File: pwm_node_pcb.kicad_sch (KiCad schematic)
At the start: 36 parts, among them J1 External Power, J2 CAN1, U1 LD1117S33CTR, U2 TJA1051T/3, U3 AP63203WU, U4 TXB0104QPWRQ1, U5 STM32L432KCU

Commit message: Add re-layout WIP changes
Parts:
- removed C7: 22p, Capacitor_SMD:C_0603_1608Metric, symbol Device:C
- removed J2: CAN1, Connector_PinHeader_2.54mm:PinHeader_1x02_P2.54mm_Vertical, symbol Connector:Conn_01x02_Pin
- removed J3: ~, tag_connect:tag_connect_tc2030-idc-nl, symbol tag_connect:tag_connect_arm_swd_tc2030-nl
- removed L1: 10u, Inductor_SMD:L_0402_1005Metric, symbol Device:L
- removed U3: AP63203WU, Package_TO_SOT_SMD:TSOT-23-6, symbol Regulator_Switching:AP63203WU
- added J2: TC2050-IDC-NL, tag_connect:tag_connect_tc2050-idc-nl, symbol tag_connect:tag_connect_arm_swd_tc2050-nl
- added R4: 76k8, Resistor_SMD:R_0603_1608Metric, symbol Device:R
- added TP1: TestPoint, TestPoint:TestPoint_Pad_D1.5mm, symbol Connector:TestPoint
- added U3: TPSM82903, ti_buck:tpsm8290x, symbol ti_buck:tpsm82903
- C3: footprint Capacitor_SMD:C_0603_1608Metric -> Capacitor_SMD:C_0805_2012Metric
- C4: value 100n -> 22u; footprint Capacitor_SMD:C_0603_1608Metric -> Capacitor_SMD:C_0805_2012Metric
- C5: value 100p -> 16n
- C6: value 22p -> 4n7
- J1: value External Power -> CAN1
- R1: value 120R -> 60R
- R2: value 158k -> 60R
- R3: value 30k1 -> 76k8
- renumbered C11 to C10, C12 to C11, C8 to C7, C9 to C8, C10 to C9, J4 to J3, R4 to R5, U5 to U4, U4 to U5
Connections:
- net +3V3: now also J2.1 (VCC)
- net +5V: now also C4.1, J3.11, J3.2, J3.5, J3.8, U3.10 (VOUT), U3.9 (VOUT); no longer C5.1, C6.1, R2.1
- net CAN1+: now also J1.1 (Pin_1), R2.1; no longer R1.1
- net CAN1-: now also J1.2 (Pin_2), R1.1; no longer R1.2
- net GND: now also C4.2, C5.2, C6.2, J2.3 (GND), J2.5 (GND/VPROG), R4.2, U3.11 (GND); no longer J1.2 (Pin_2)
- net NRST: now also J2.10 (~{RESET})
- net SWCLK: now also J2.4 (SWCLK/TCK)
- net SWDIO: now also J2.2 (SWDIO/TMS)
- net SWO: now also J2.6 (SWO/TDO)
- removed net +V_{L}: C3.1, J1.1 (Pin_1), J3.11, J3.2, J3.5, J3.8
- new net: C6.1, R1.2, R2.2
- new net: TP1.1, U3.6 (PG)
- new net: C5.1, U3.5 (SS/TR)
- new net: R4.1, U3.4 (MODE/S-CONF)
- new net: R3.1, U3.7 (FB/VSET)
- new net +VSUPPLY: C3.1, U3.1 (VIN), U3.2 (VIN), U3.3 (EN)
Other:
- note added: "5V Buck Converter"
- note added: "MODE/S-CONFIG Resistor Setting: - FB/VSET-Pin: VSET mode - R_{MODE/S-CONF} = 76.8kΩ - F_{SW} = 1 MHz - Output discharge: Yes - Mode: Forced PWM - Dynamic mode change: Not active"
- note added: "Resistors: E96 Resistor Series, 1% Accuracy, Temperature Coefficient better or equal than ±200 ppm/°C C_{VIN} suggested: 0805 C_{VOUT} suggested: 0805"
- note added: "Soft start time C_{SS} = T_{SS} * I_{SS} / V_{REF} I_{SS} = 2.5uA V_{REF} = V_{FB}/0.75 V_{REF} = 0.6V / 0.75 = 0.8V For T_{SS} = 5ms: C_{SS} = 15.625nF"
- note added: "VSET Mode (5V) - R_{VSET} = 76.8kΩ"
- note removed: "Load Power Supply and to 5V"
- moved on the sheet: C10, C11, C7, C8, C9, JP1, JP2, R5, U4, U5

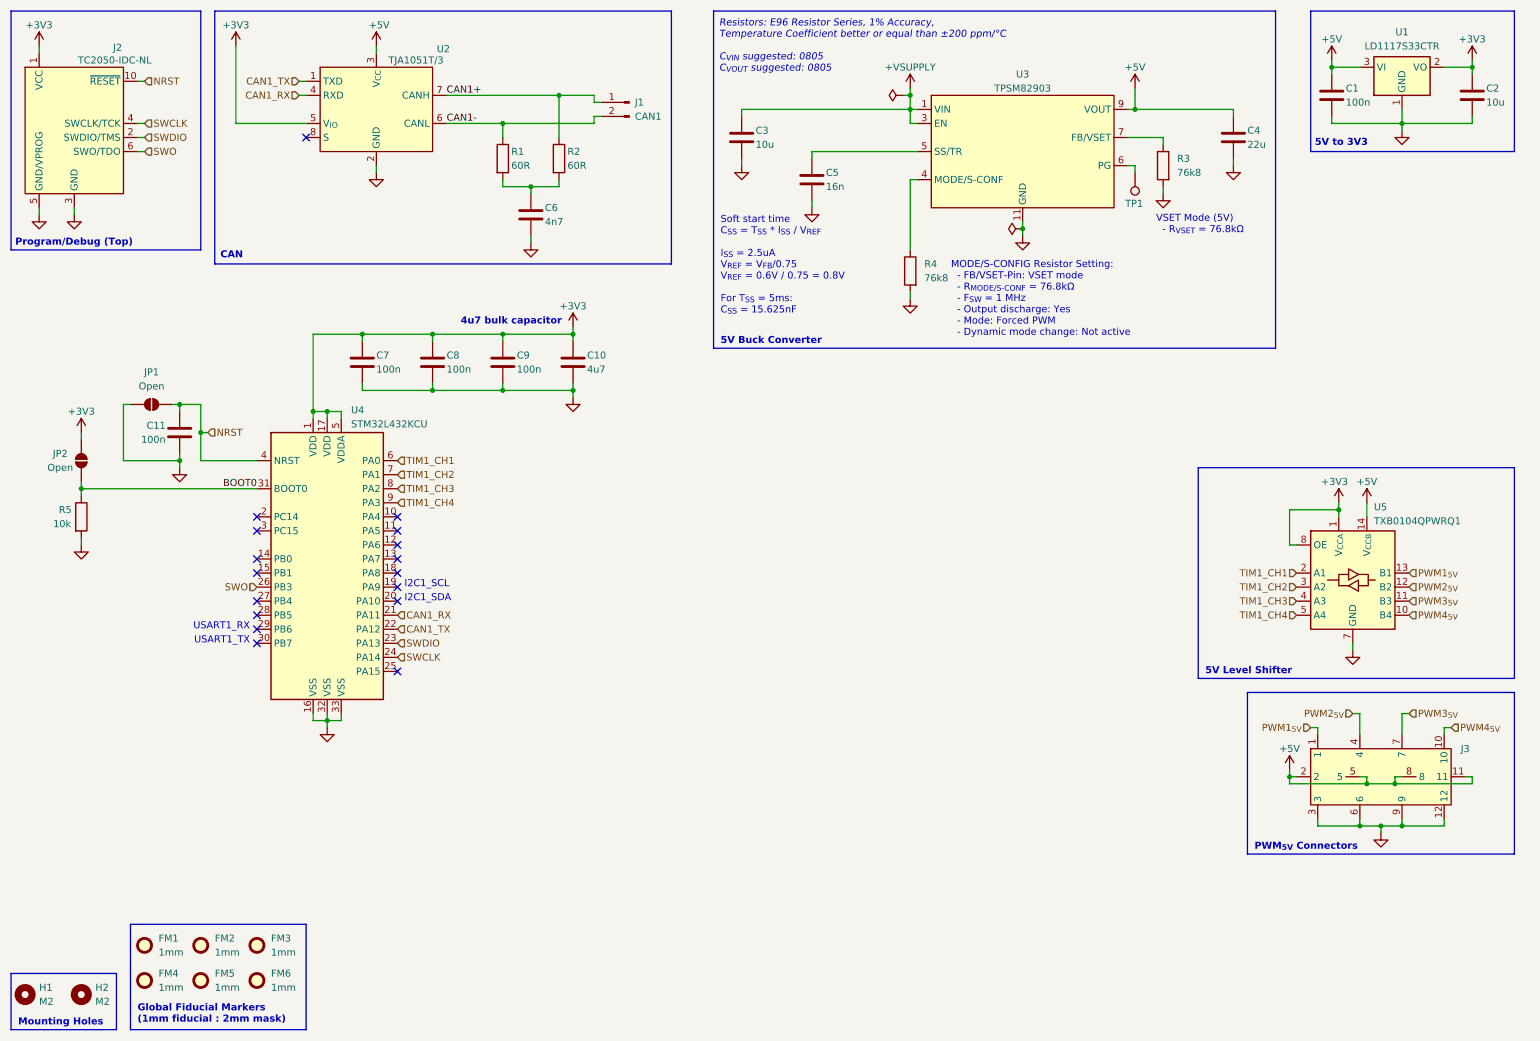
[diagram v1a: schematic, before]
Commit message: Revamp schematic and nuke PCB
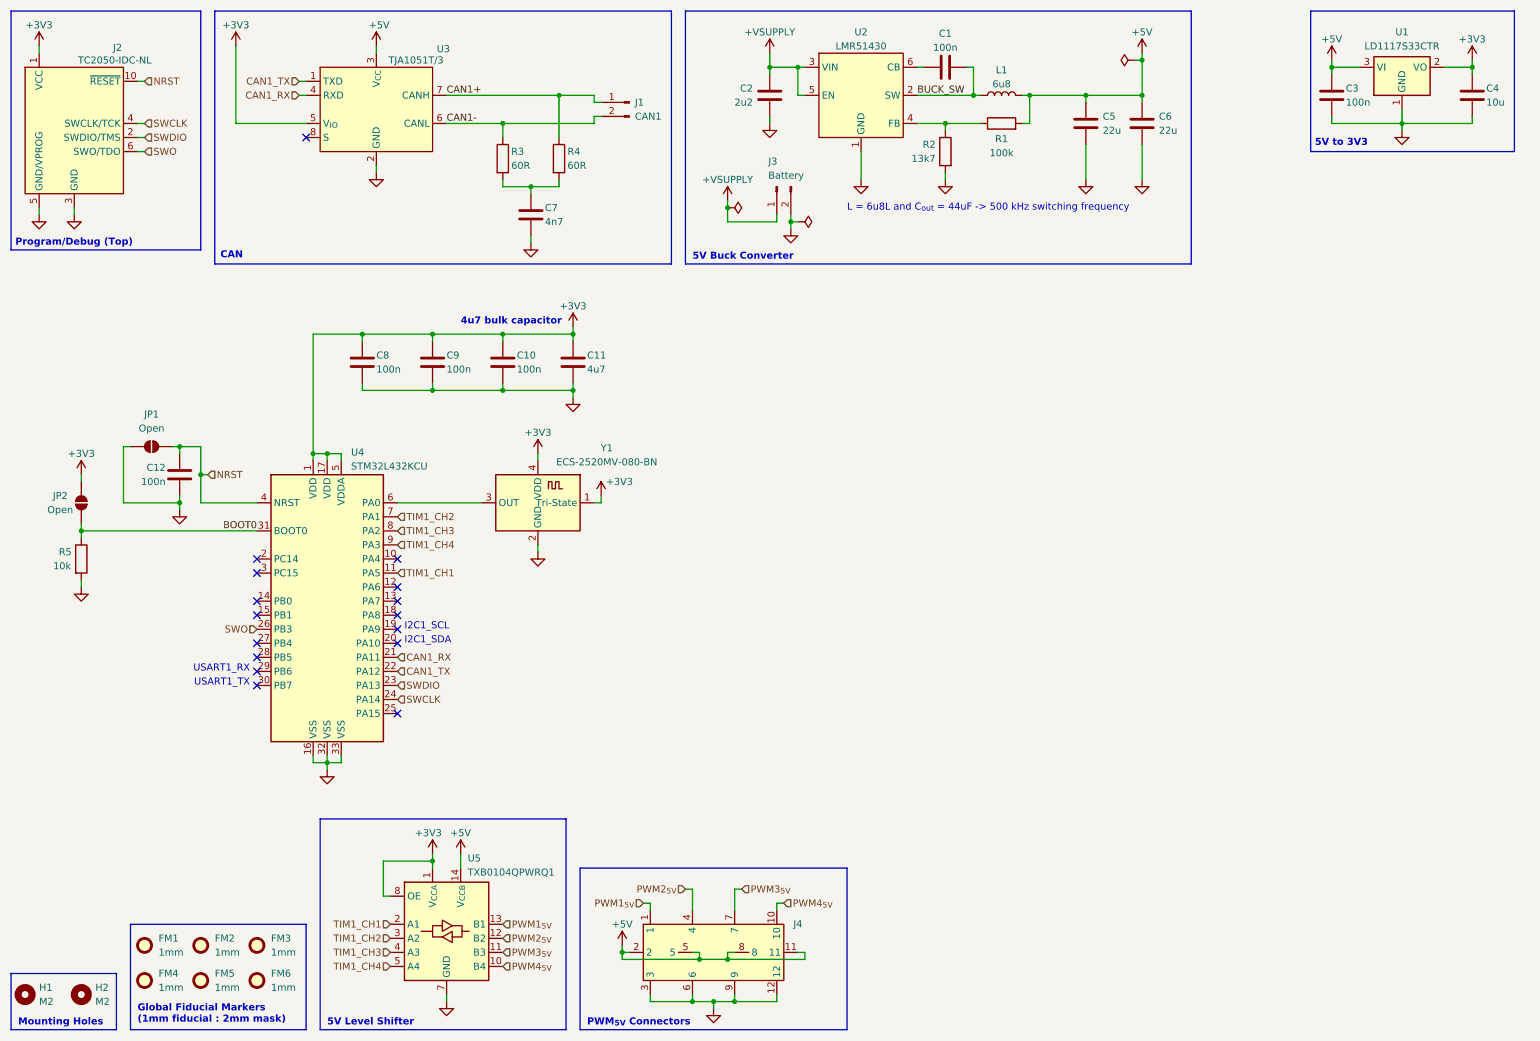
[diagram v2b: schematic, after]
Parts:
- removed C3: 10u, Capacitor_SMD:C_0805_2012Metric, symbol Device:C
- removed C4: 22u, Capacitor_SMD:C_0805_2012Metric, symbol Device:C
- removed J3: ~, pwm_node_connector:3x4_2-54mm_breakout, symbol pwm_node_connector:3x4_2-54mm_breakout
- removed R3, R4: 76k8, Resistor_SMD:R_0603_1608Metric, symbol Device:R
- removed TP1: TestPoint, TestPoint:TestPoint_Pad_D1.5mm, symbol Connector:TestPoint
- removed U3: TPSM82903, ti_buck:tpsm8290x, symbol ti_buck:tpsm82903
- added C1: 100n, Capacitor_SMD:C_0805_2012Metric, symbol Device:C
- added C2: 2u2, Capacitor_SMD:C_0805_2012Metric, symbol Device:C
- added C6: 22u, Capacitor_SMD:C_1210_3225Metric, symbol Device:C
- added J3: Battery, pwm_node_connectors:battery, symbol Connector:Conn_01x02_Pin
- added J4: ~, pwm_node_connectors:3x4_2-54mm_breakout, symbol pwm_connector_3x4_2-54mm_breakout:3x4_2-54mm_breakout
- added L1: 6u8, pwm_node_inductor:vishay_ihlp-2525cz, symbol Device:L
- added R1: 100k, Resistor_SMD:R_0603_1608Metric, symbol Device:R
- added R2: 13k7, Resistor_SMD:R_0603_1608Metric, symbol Device:R
- added U2: LMR51430, ti_buck:lmr51430, symbol ti_buck:lmr51430
- added Y1: ECS-2520MV-080-BN, Oscillator:Oscillator_SMD_ECS_2520MV-xxx-xx-4Pin_2.5x2.0mm, symbol Oscillator:ECS-2520MV-xxx-xx
- C5: value 16n -> 22u; footprint Capacitor_SMD:C_0603_1608Metric -> Capacitor_SMD:C_1210_3225Metric
- U4: Manufacturer Part Number STM32L432KC -> STM32L432KCU6
- renumbered C9 to C10, C10 to C11, C11 to C12, C1 to C3, C2 to C4, C6 to C7, C7 to C8, C8 to C9, R1 to R3, R2 to R4, U2 to U3
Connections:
- net +3V3: now also Y1.1 (Tri-State), Y1.4 (VDD)
- net +5V: now also C5.2, C6.2, J4.11, J4.2, J4.5, J4.8, L1.2, R1.2
- net +VSUPPLY: now also C2.1, J3.1 (Pin_1), U2.3 (VIN), U2.5 (EN)
- net GND: now also C5.1, C2.2, C6.1, J3.2 (Pin_2), J4.12, J4.3, J4.6, J4.9, R2.2, U2.1 (GND), Y1.2 (GND); no longer C5.2
- net PWM1_{5V}: now also J4.1
- net PWM2_{5V}: now also J4.4
- net PWM3_{5V}: now also J4.7
- net PWM4_{5V}: now also J4.10
- net TIM1_CH1: now also U4.11 (PA5); no longer U4.6 (PA0)
- new net: R1.1, R2.1, U2.4 (FB)
- new net: U4.6 (PA0), Y1.3 (OUT)
- new net: C1.1, U2.6 (CB)
- new net BUCK_SW: C1.2, L1.1, U2.2 (SW)
- no-connect marks 17 -> 16
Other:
- note added: "L = 6u8L and C_{out} = 44uF -> 500 kHz switching frequency"
- note removed: "MODE/S-CONFIG Resistor Setting: - FB/VSET-Pin: VSET mode - R_{MODE/S-CONF} = 76.8kΩ - F_{SW} = 1 MHz - Output discharge: Yes - Mode: Forced PWM - Dynamic mode change: Not active"
- note removed: "Resistors: E96 Resistor Series, 1% Accuracy, Temperature Coefficient better or equal than ±200 ppm/°C C_{VIN} suggested: 0805 C_{VOUT} suggested: 0805"
- note removed: "Soft start time C_{SS} = T_{SS} * I_{SS} / V_{REF} I_{SS} = 2.5uA V_{REF} = V_{FB}/0.75 V_{REF} = 0.6V / 0.75 = 0.8V For T_{SS} = 5ms: C_{SS} = 15.625nF"
- note removed: "VSET Mode (5V) - R_{VSET} = 76.8kΩ"
- moved on the sheet: C12, JP1, JP2, R5, U4, U5

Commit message: Initial component placement
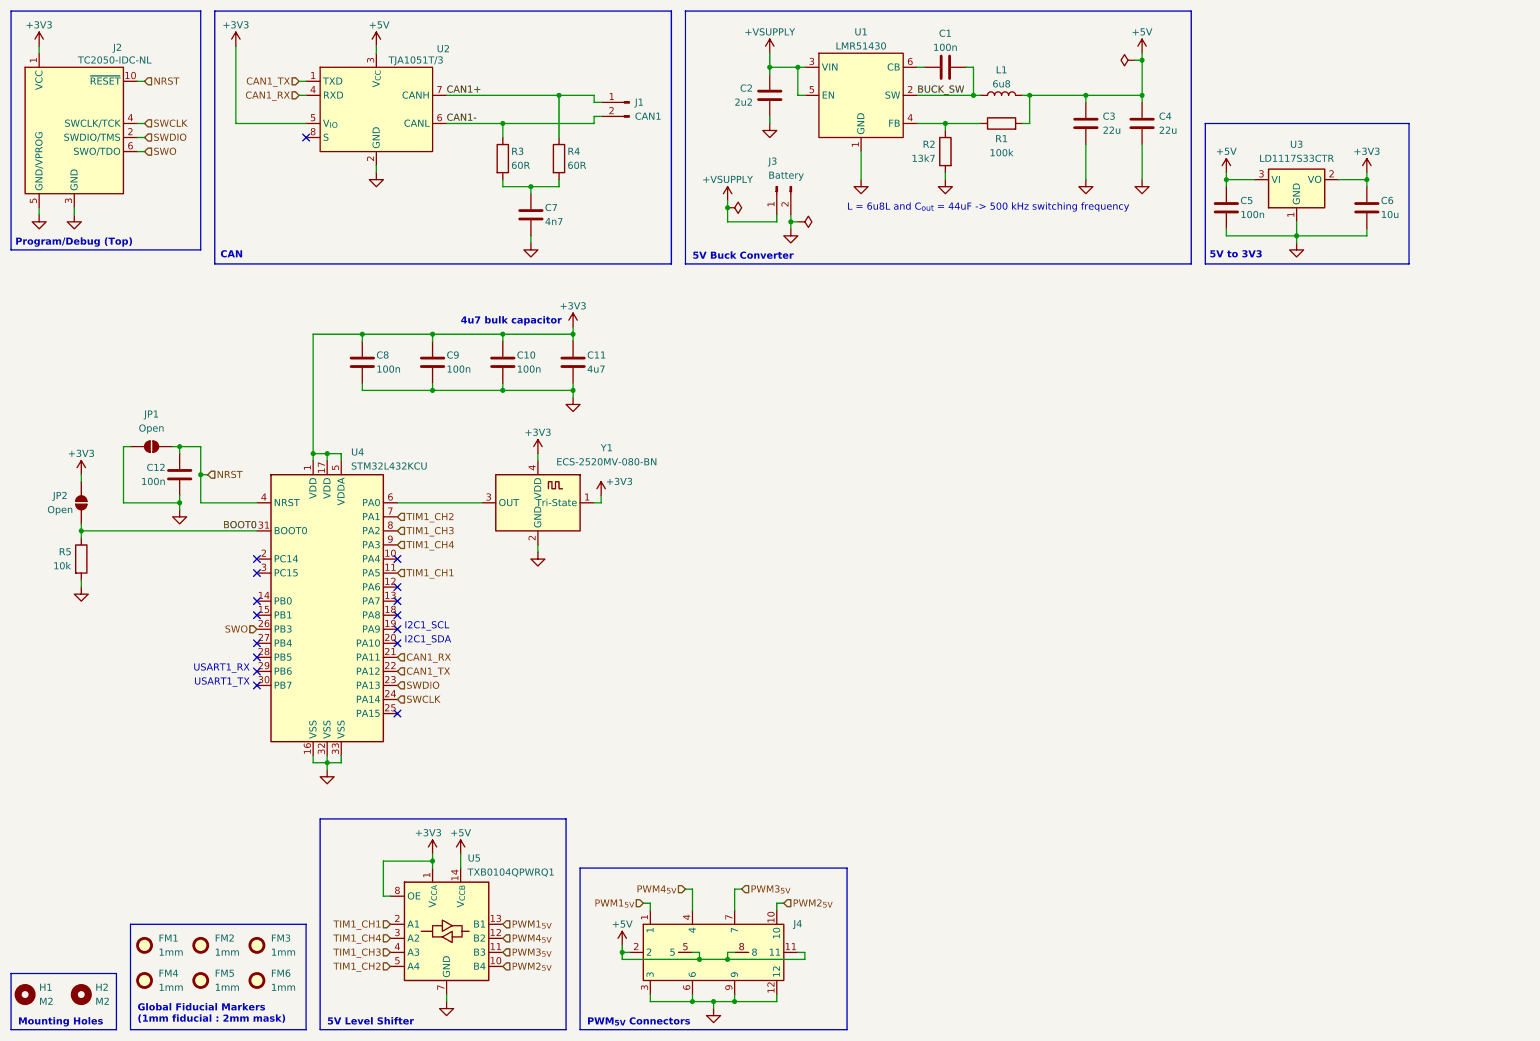
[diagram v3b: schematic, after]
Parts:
- renumbered C5 to C3, C6 to C4, C3 to C5, C4 to C6, U2 to U1, U3 to U2, U1 to U3
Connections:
- net PWM2_{5V}: now also J4.10, U5.10 (B4); no longer J4.4, U5.12 (B2)
- net PWM4_{5V}: now also J4.4, U5.12 (B2); no longer J4.10, U5.10 (B4)
- net TIM1_CH2: now also U5.5 (A4); no longer U5.3 (A2)
- net TIM1_CH4: now also U5.3 (A2); no longer U5.5 (A4)
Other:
- moved on the sheet: C5, C6, U3

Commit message: Split load supply and rough placement
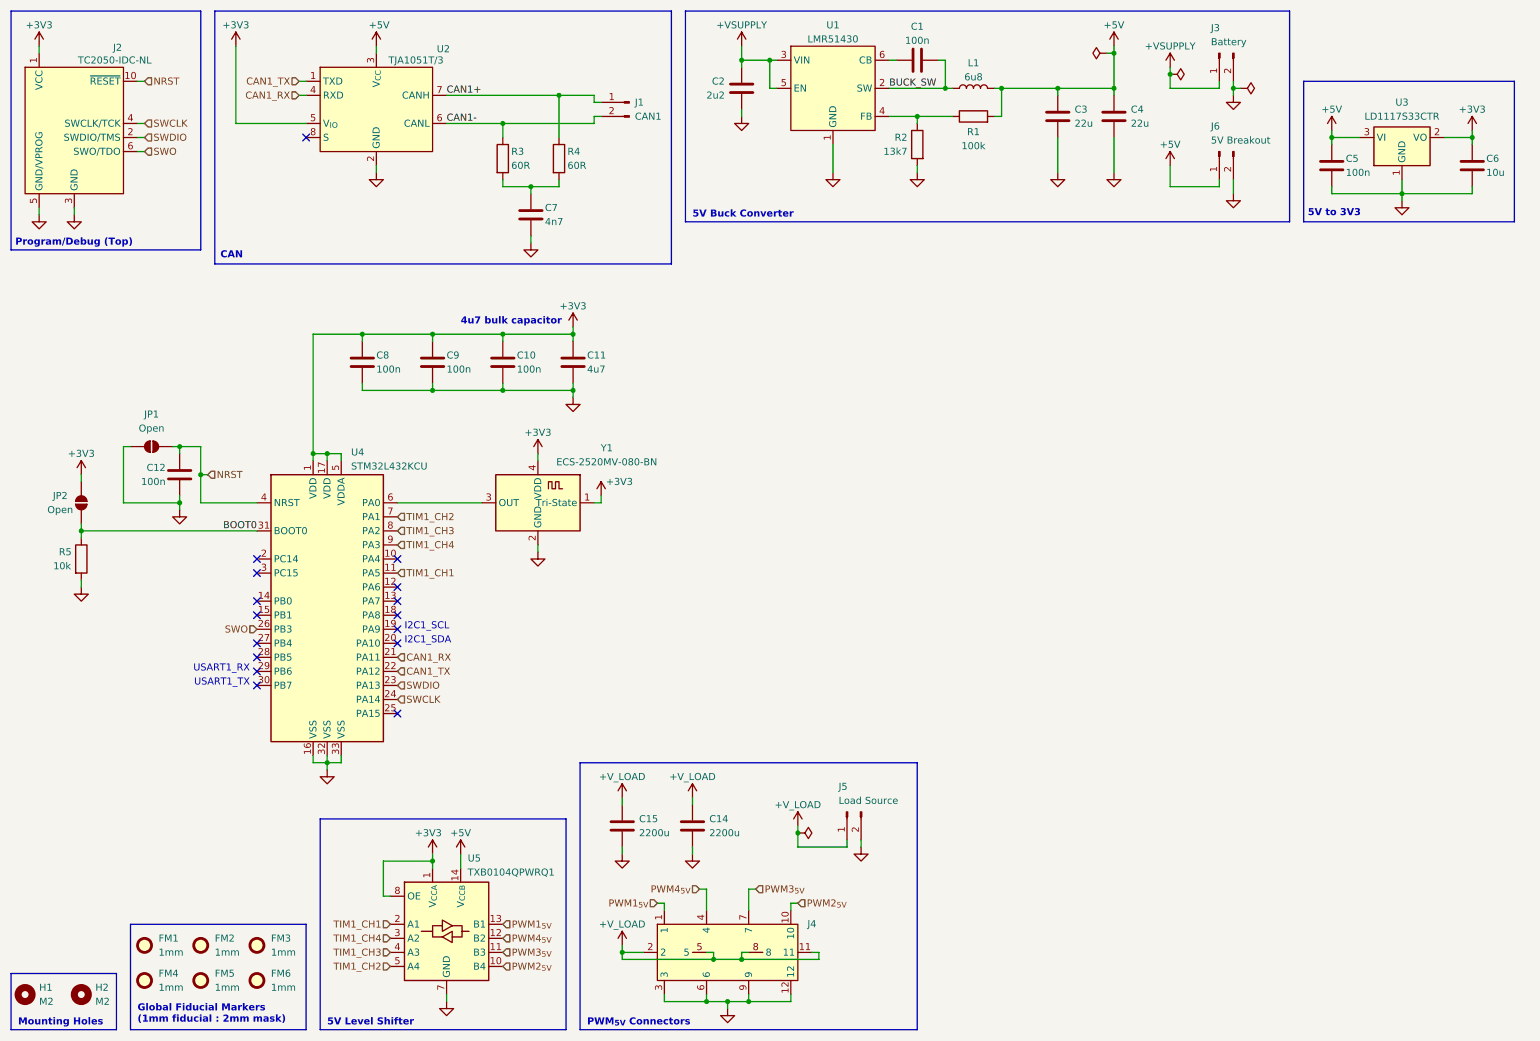
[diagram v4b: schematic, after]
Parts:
- added C14, C15: 2200u, Capacitor_SMD:C_Elec_3x5.4, symbol Device:C
- added J5: Load Source, pwm_node_connectors:battery, symbol Connector:Conn_01x02_Pin
- added J6: 5V Breakout, pwm_node_connectors:battery, symbol Connector:Conn_01x02_Pin
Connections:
- net +5V: now also J6.1 (Pin_1); no longer J4.11, J4.2, J4.5, J4.8
- net GND: now also C14.1, C15.1, J5.2 (Pin_2), J6.2 (Pin_2)
- new net +V_LOAD: C14.2, C15.2, J4.11, J4.2, J4.5, J4.8, J5.1 (Pin_1)
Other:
- note removed: "L = 6u8L and C_{out} = 44uF -> 500 kHz switching frequency"
- moved on the sheet: C1, C2, C3, C4, C5, C6, J3, J4, L1, R1, R2, U1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

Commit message: Pass ERC and DRC, initial v0.1.0-alpha
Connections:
- net +3V3: now also JP2.1 (A); no longer JP2.2 (B)
- net BOOT0: now also JP2.2 (B); no longer JP2.1 (A)
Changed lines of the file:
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@@
 		(lib_id "Jumper:SolderJumper_2_Open")
 		(at 25.4 101.6 90)
+		(mirror x)
 		(unit 1)
 		(exclude_from_sim no)
@@
 		(dnp no)
 		(property "Reference" "JP2"
-			(at 21.59 100.33 90)
+			(at 21.59 102.87 90)
 			(effects
 				(font
@@
 		)
 		(property "Value" "Open"
-			(at 21.59 102.87 90)
+			(at 21.59 100.33 90)
 			(effects
 				(font
